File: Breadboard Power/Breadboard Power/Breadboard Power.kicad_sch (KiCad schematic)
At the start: 32 parts, among them J1 Barrel_Jack, J2 Conn_02x05_Odd_Even, J3 Conn_02x05_Odd_Even, J4 Conn_02x08_Odd_Even, J5 Conn_02x08_Odd_Even, U1 LT1963, U2 LT3015

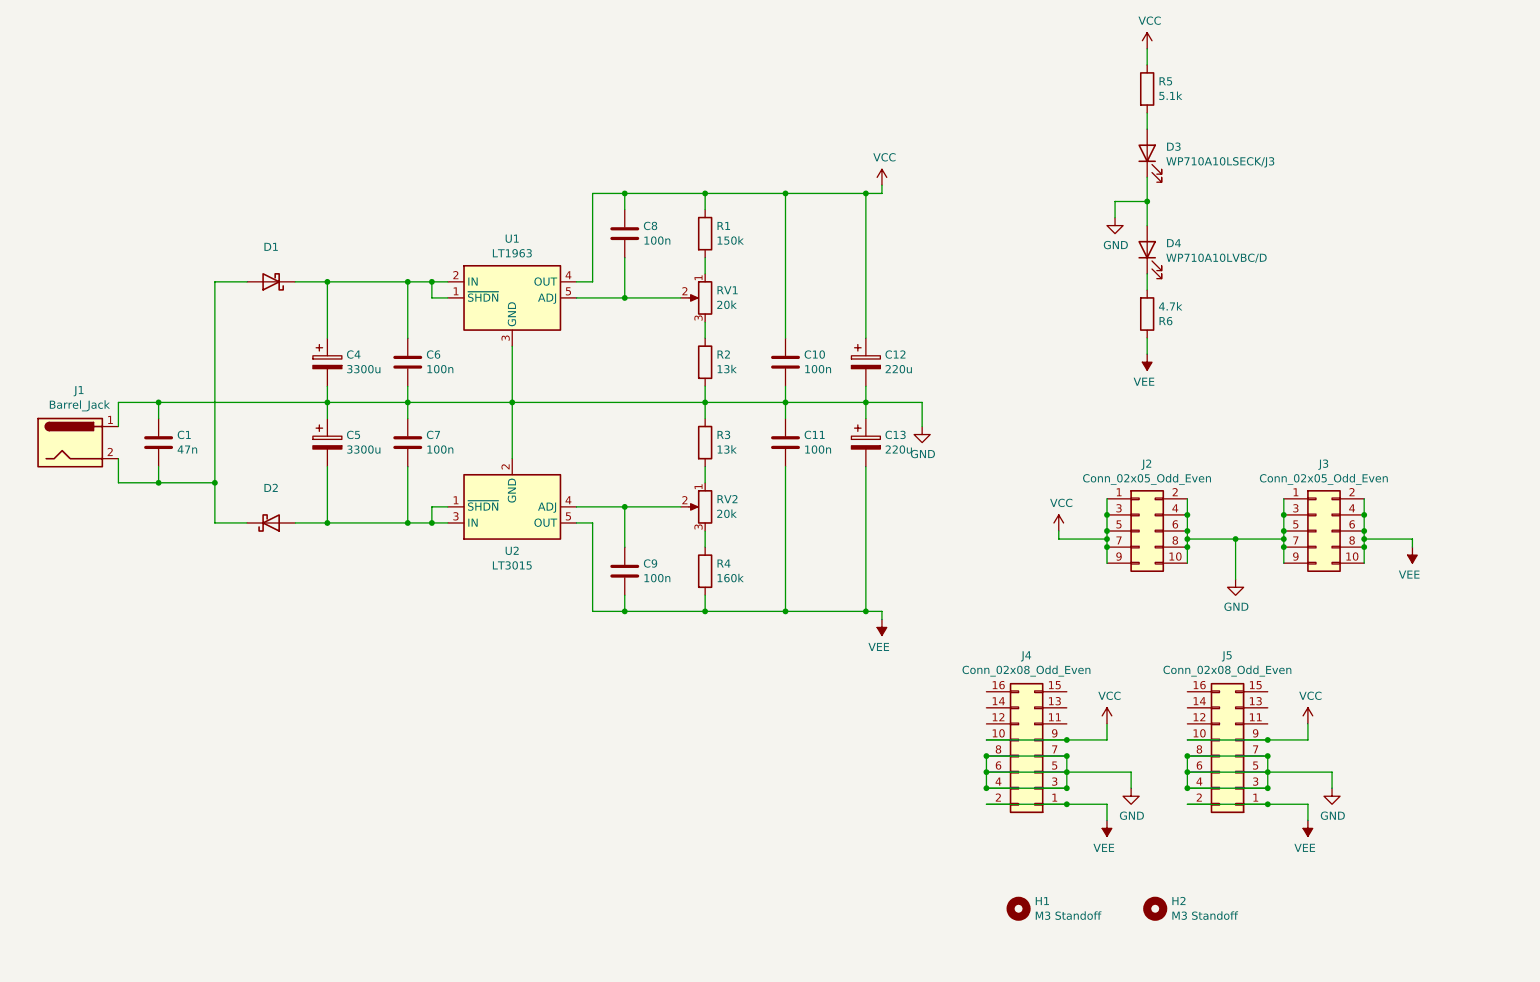
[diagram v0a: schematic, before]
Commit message: updated breadboard power to REV 3
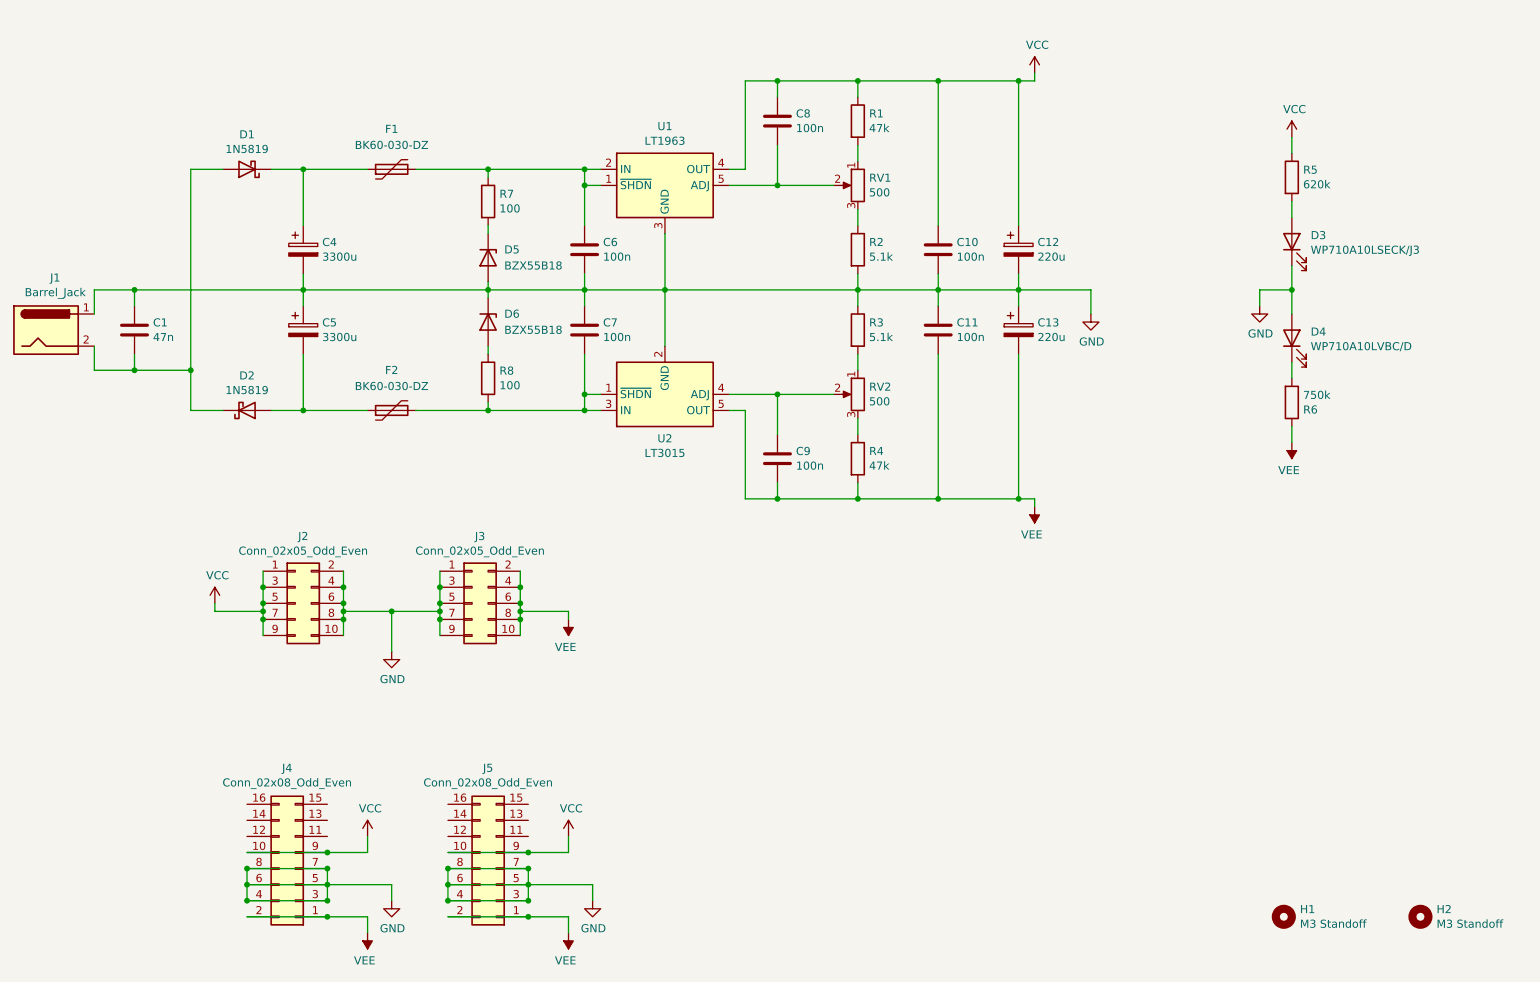
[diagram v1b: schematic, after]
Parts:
- added D5, D6: BZX55B18, Diode_THT:D_DO-35_SOD27_P7.62mm_Horizontal, symbol Device:D_Zener
- added F1, F2: BK60-030-DZ, Capacitor_THT:C_Disc_D7.5mm_W2.5mm_P5.00mm, symbol Device:Polyfuse
- added R7, R8: 100, Resistor_THT:R_Axial_DIN0207_L6.3mm_D2.5mm_P7.62mm_Horizontal, symbol Device:R
- C1: footprint NSI Footprints:C_Disc_D4mm_W2.6mm_P5.08mm -> Capacitor_THT:C_Disc_D4.7mm_W2.5mm_P5.00mm
- C10, C11, C6, C7, C8, C9: footprint NSI Footprints:C_Disc_D4mm_W2.6mm_P5.08mm -> Capacitor_THT:C_Disc_D5.0mm_W2.5mm_P5.00mm
- D1, D2: value (none) -> 1N5819
- R1: value 150k -> 47k
- R2, R3: value 13k -> 5.1k
- R4: value 160k -> 47k
- R5: value 5.1k -> 620k; footprint Resistor_THT:R_Axial_DIN0207_L6.3mm_D2.5mm_P2.54mm_Vertical -> Resistor_THT:R_Axial_DIN0207_L6.3mm_D2.5mm_P7.62mm_Horizontal
- R6: value 4.7k -> 750k; footprint Resistor_THT:R_Axial_DIN0207_L6.3mm_D2.5mm_P2.54mm_Vertical -> Resistor_THT:R_Axial_DIN0207_L6.3mm_D2.5mm_P7.62mm_Horizontal
- RV1, RV2: value 20k -> 500; footprint NSI Footprints:Potentiometer_TT_67Y_Vertical -> Potentiometer_THT:Potentiometer_Bourns_3296Y_Vertical
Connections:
- net GND: now also D5.2 (A), D6.1 (K)
- net at C6.1, U1.1 (~{SHDN}), U1.2 (IN): now also F1.2, R7.1; no longer C4.1, D1.1 (K)
- net at C7.2, U2.1 (~{SHDN}), U2.3 (IN): now also F2.2, R8.2; no longer C5.2, D2.2 (A)
- new net: C4.1, D1.1 (K), F1.1
- new net: C5.2, D2.2 (A), F2.1
- new net: D5.1 (K), R7.2
- new net: D6.2 (A), R8.1
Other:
- moved on the sheet: C1, C10, C11, C12, C13, C4, C5, C6, C7, C8, C9, D1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
